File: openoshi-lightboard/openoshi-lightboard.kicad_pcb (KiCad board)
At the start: 2 copper layers, 30 x 30 mm, 26 parts, among them J1 USB_C_Receptacle_PowerOnly_6P, Q1 CSD16301Q2, Q2 CSD16301Q2, Q3 CSD16301Q2, Q4 CSD16301Q2, SW1 SW_Push, SW2 SW_Push, U1 CH32V003FxUx, U2 TLV61070ADBV, U3 MCP73831-3-MC

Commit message: added pictures to readme
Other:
- board text added: "OpenOshi Lightboard v2.0"
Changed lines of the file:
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@@
 			(at 0 3.5 0)
 			(layer "B.SilkS")
+			(hide yes)
 			(effects
 				(font
@@
 		(layer "Edge.Cuts")
 	)
+	(gr_text "OpenOshi Lightboard v2.0"
+		(at 151.65 85.4 0)
+		(layer "B.SilkS")
+		(effects
+			(font
+				(size 0.5 0.5)
+				(thickness 0.1)
+				(bold yes)
+			)
+			(justify left bottom mirror)
+		)
+	)
 	(zone

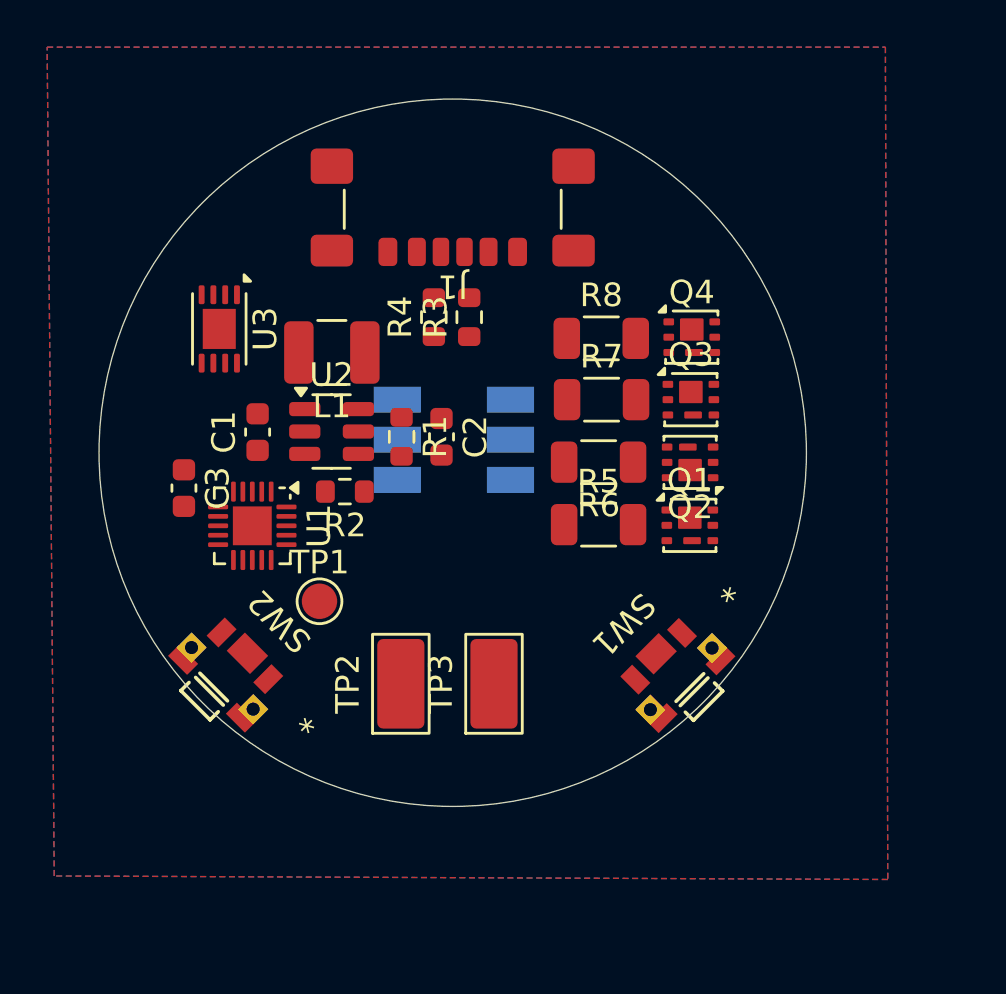
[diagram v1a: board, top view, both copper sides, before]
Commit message: updated readme and part names
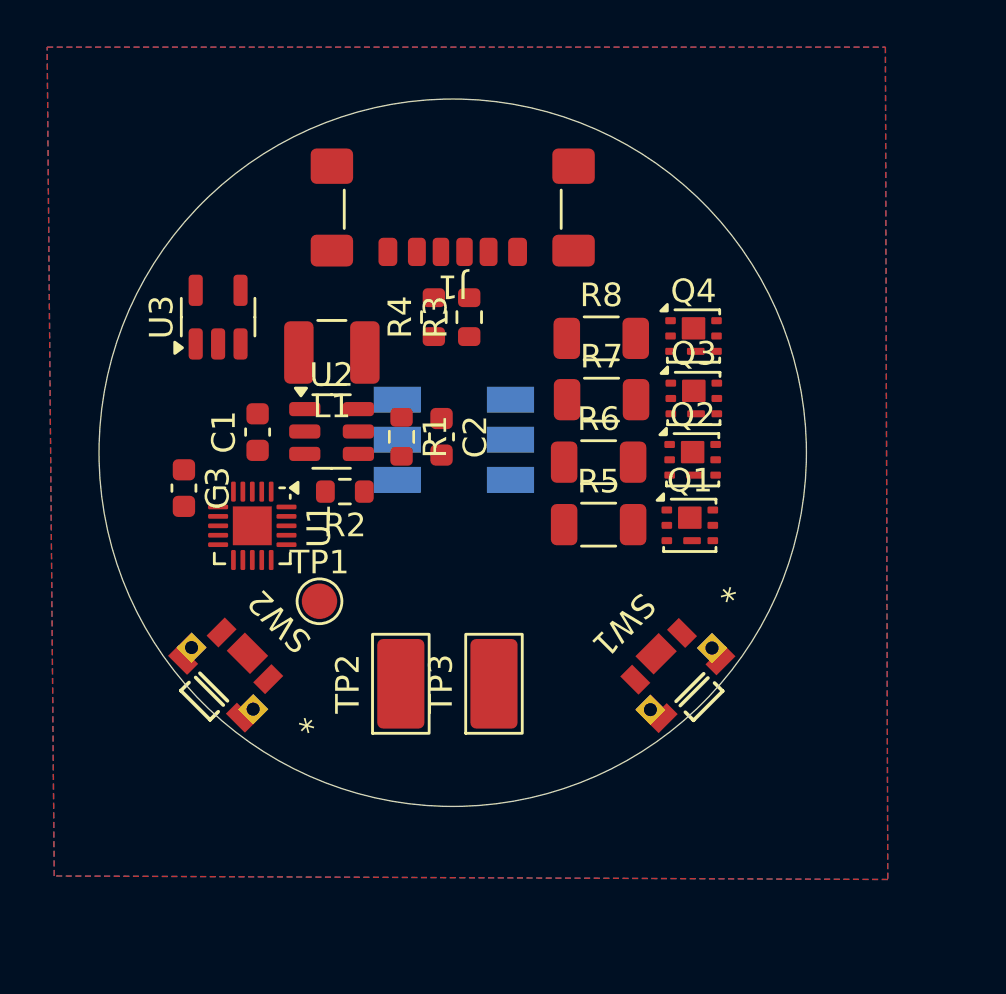
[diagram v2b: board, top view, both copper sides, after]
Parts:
- Q1, Q2, Q3, Q4: value CSD16301Q2 -> CSD17318Q2
- U3: value MCP73831-3-MC -> MCP73831-2-OT; footprint Package_DFN_QFN:DFN-8-1EP_3x2mm_P0.5mm_EP1.7x1.4mm -> Package_TO_SOT_SMD:SOT-23-5
- moved U3 0.50 mm to (136.7, 91.2), turned to 90 degrees
- moved Q2 0.15 mm to (156.8, 97.2), turned to 0 degrees
- moved Q3 0.13 mm to (156.8, 94.6)
- moved Q4 0.09 mm to (156.8, 92.0)
- turned R6 to 0 degrees
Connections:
- U3 pad 1: VBUS -> unconnected-(U3-STAT-Pad1)
- U3 pad 2: VBUS -> GND
- U3 pad 4: +BATT -> VBUS
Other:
- rule pad_to_mask_clearance: 0 -> 0.038

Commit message: added LED
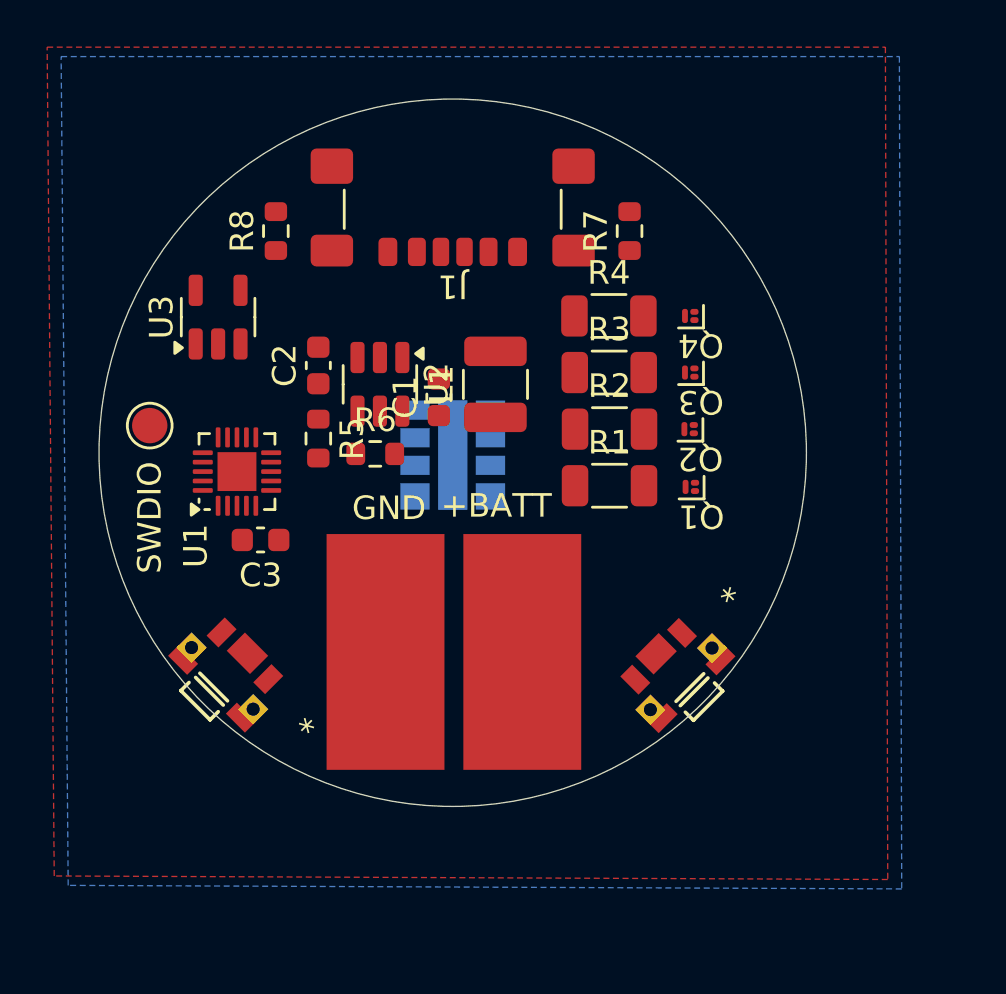
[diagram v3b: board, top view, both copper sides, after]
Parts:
- removed D1: APA102, LED_SMD:LED_RGB_5050-6
- added LED1: L1MC-RGB5080500MP0, openoshi-lightboard:5050RGBW_LUL, B.Cu at (146.6, 97.0)
- L1: value L -> 4.7uH
- Q1, Q2, Q3, Q4: value CSD17318Q2 -> CSD17484F4; footprint Package_SON:Texas_DQK -> Package_DFN_QFN:Texas_PicoStar_DFN-3_0.69x0.60mm
- TP2: value TestPoint -> +BATT; footprint TestPoint:TestPoint_Keystone_5019_Miniature -> Connector_Wire:SolderWirePad_1x01_SMD_5x10mm
- TP3: value TestPoint -> GND; footprint TestPoint:TestPoint_Keystone_5019_Miniature -> Connector_Wire:SolderWirePad_1x01_SMD_5x10mm
- moved TP1 10.4 mm to (133.8, 95.8)
- moved C1 7.83 mm to (146.0, 94.5)
- moved R7 7.72 mm to (154.1, 87.5)
- moved R8 7.63 mm to (139.1, 87.5)
- moved L1 7.07 mm to (148.4, 94.0), turned to 90 degrees
- moved C2 6.04 mm to (140.9, 93.2), turned to 90 degrees
- moved TP2 5.32 mm to (149.6, 105.3), turned to 180 degrees
- moved TP3 4.79 mm to (143.8, 105.3), turned to 180 degrees
- moved C3 3.92 mm to (138.4, 100.6), turned to 0 degrees
- moved R5 3.53 mm to (140.9, 96.3)
- moved U2 2.86 mm to (143.5, 94.0), turned to -90 degrees
- moved U1 2.39 mm to (137.4, 97.7), turned to 90 degrees
- moved R6 2.05 mm to (143.3, 97.0), turned to 0 degrees
- moved R1 1.71 mm to (153.2, 98.3)
- moved Q1 1.63 mm to (156.7, 98.3), turned to 180 degrees
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- renumbered R5 to R1, R6 to R2, R7 to R3, R8 to R4, R1 to R5, R2 to R6, R3 to R7, R4 to R8
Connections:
- net Net-(U2-V_{FB}) renamed /VREG_FB
- Q1 pad 1: Net-(Q1-D-Pad1) -> /G_BLUE
- Q1 pad 2: Net-(Q1-D-Pad1) -> GND
- Q1 pad 3: unconnected-(Q1-G-Pad3) -> Net-(Q1-D)
- Q2 pad 1: Net-(Q2-D-Pad1) -> /G_RED
- Q2 pad 2: Net-(Q2-D-Pad1) -> GND
- Q2 pad 3: unconnected-(Q2-G-Pad3) -> Net-(Q2-D)
- Q3 pad 1: Net-(Q3-D-Pad1) -> /G_GREEN
- Q3 pad 2: Net-(Q3-D-Pad1) -> GND
- Q3 pad 3: unconnected-(Q3-G-Pad3) -> Net-(Q3-D)
- Q4 pad 1: Net-(Q4-D-Pad1) -> /G_WHITE
- Q4 pad 2: Net-(Q4-D-Pad1) -> GND
- Q4 pad 3: unconnected-(Q4-G-Pad3) -> Net-(Q4-D)
- R1 pad 1: unconnected-(R5-Pad1) -> /K_BLUE
- R1 pad 2: Net-(Q1-D-Pad1) -> Net-(Q1-D)
- R2 pad 1: unconnected-(R6-Pad1) -> /K_RED
- R2 pad 2: Net-(Q2-D-Pad1) -> Net-(Q2-D)
- R3 pad 1: unconnected-(R7-Pad1) -> /K_GREEN
- R3 pad 2: Net-(Q3-D-Pad1) -> Net-(Q3-D)
- R4 pad 1: unconnected-(R8-Pad1) -> /K_WHITE
- R4 pad 2: Net-(Q4-D-Pad1) -> Net-(Q4-D)

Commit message: Safety upgrades all around
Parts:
- removed LED1: L1MC-RGB5080500MP0, openoshi-lightboard:5050RGBW_LUL
- added D1: Lumileds_5052RGBW, openoshi-lightboard:LED_Lumileds_5052RGBW_LGA9_5.0x5.2mm_P0.5mm, F.Cu at (150.4, 98.4)
- added R10: 2k, Resistor_SMD:R_0603_1608Metric, F.Cu at (154.4, 97.3)
- added R9: 220, Resistor_SMD:R_0603_1608Metric, F.Cu at (158.3, 97.1)
- J1: footprint Connector_USB:USB_C_Receptacle_GCT_USB4135-GF-A_6P_TopMnt_Horizontal -> Connector_USB:USB_C_Receptacle_GCT_USB4125-xx-x_6P_TopMnt_Horizontal
- L1: value 4.7uH -> L
- Q1, Q2, Q3, Q4: value CSD17484F4 -> PMZ600UNEYL
- R5: renamed from R1; value R -> 118; footprint Resistor_SMD:R_1206_3216Metric -> Resistor_SMD:R_0603_1608Metric
- R6: renamed from R2; value R -> 69.8; footprint Resistor_SMD:R_1206_3216Metric -> Resistor_SMD:R_0603_1608Metric
- R7: renamed from R3; value R -> 69.8; footprint Resistor_SMD:R_1206_3216Metric -> Resistor_SMD:R_0603_1608Metric
- R8: renamed from R4; value R -> 69.8; footprint Resistor_SMD:R_1206_3216Metric -> Resistor_SMD:R_0603_1608Metric
- TP2, TP3: footprint Connector_Wire:SolderWirePad_1x01_SMD_5x10mm -> TestPoint:TestPoint_Keystone_5019_Miniature; moved to B.Cu
- U2: value TLV61070ADBV -> TLV61220
- moved TP1 25.4 mm to (159.2, 95.0), turned to 135 degrees
- moved U1 18.8 mm to (156.1, 100.2), turned to 0 degrees
- moved Q4 18.4 mm to (147.3, 107.0), turned to 90 degrees
- moved U3 18.0 mm to (154.3, 94.8), turned to 180 degrees
- moved C3 17.1 mm to (155.2, 104.0), turned to 90 degrees
- moved Q3 15.5 mm to (148.9, 107.0), turned to 90 degrees
- moved R8 14.8 mm to (147.3, 104.7), turned to -90 degrees
- moved Q2 12.6 mm to (150.6, 107.0), turned to 90 degrees
- moved R7 12.0 mm to (148.9, 104.7), turned to -90 degrees
- moved R4 11.8 mm to (149.2, 93.8)
- moved Q1 9.68 mm to (152.2, 106.9), turned to 90 degrees
- moved TP3 9.38 mm to (151.3, 99.8), turned to 90 degrees
- moved R6 9.19 mm to (150.6, 104.7), turned to -90 degrees
- moved C1 7.81 mm to (139.7, 99.2)
- moved R3 7.09 mm to (150.8, 93.8)
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- renumbered R5 to R1, R6 to R2, R7 to R3, R8 to R4
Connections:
- net /VREG_FB renamed Net-(U2-V_{FB})
- SW1 pad 1: unconnected-(SW1-Pad1) -> /SW1_DET
- SW1 pad 2: unconnected-(SW1-Pad2) -> GND
- SW2 pad 1: unconnected-(SW2-Pad1) -> /SW2_DET
- SW2 pad 2: unconnected-(SW2-Pad2) -> GND
- U1 pad 15: /SWDIO -> Net-(U1-PD1)
- U3 pad 1: unconnected-(U3-STAT-Pad1) -> /CHG_STAT
- U3 pad 5: unconnected-(U3-PROG-Pad5) -> Net-(U3-PROG)
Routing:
- net GND: vias 0 -> 1

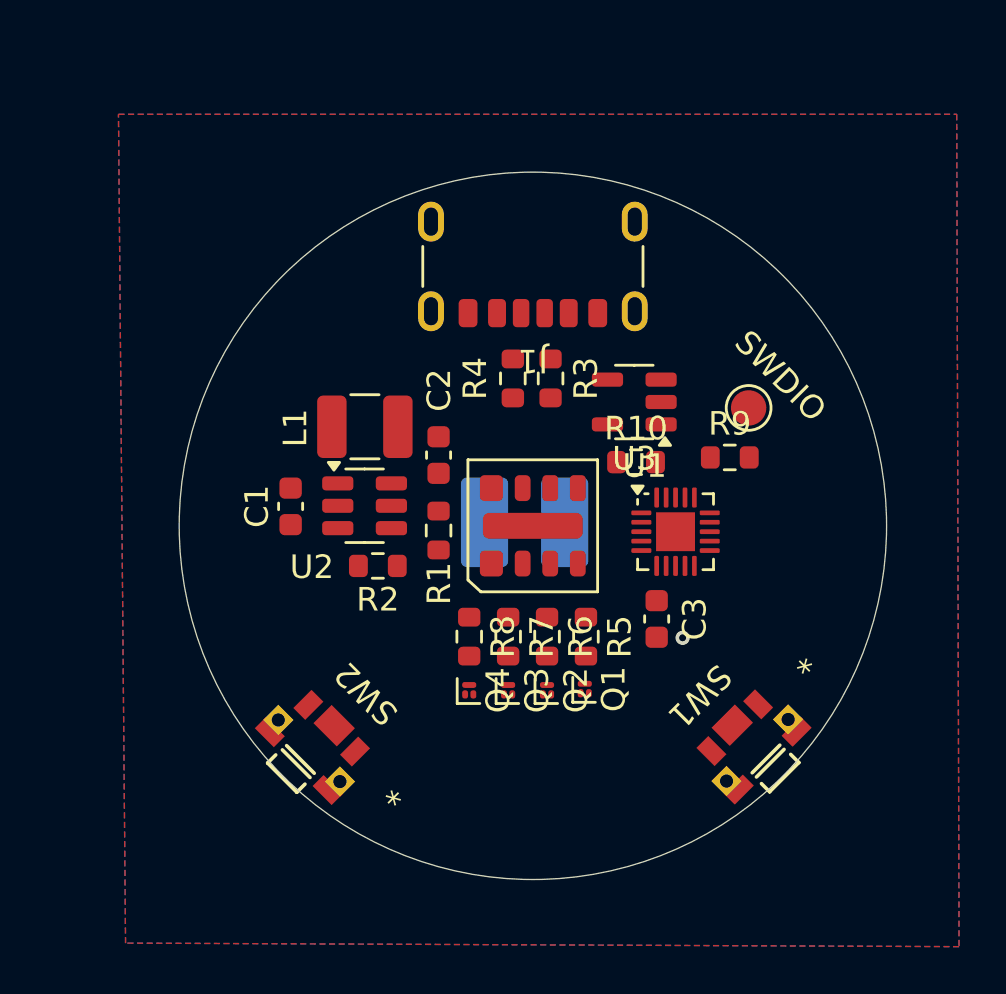
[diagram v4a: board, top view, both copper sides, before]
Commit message: Tentative sch completion, initial layout
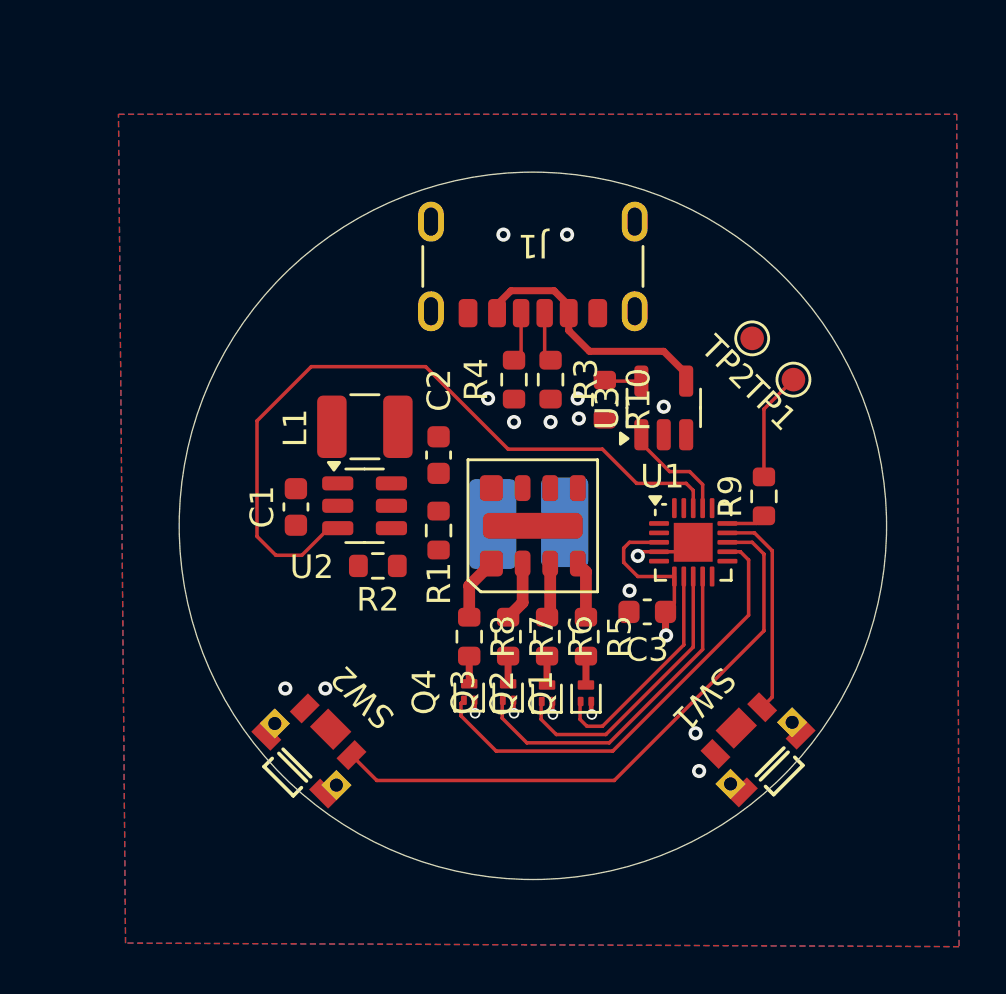
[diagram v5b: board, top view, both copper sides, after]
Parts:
- added TP4: GND, TestPoint:TestPoint_Keystone_5019_Miniature, B.Cu at (148.3, 99.9)
- L1: value L -> 4.7uH
- Q1, Q2, Q3, Q4: value PMZ600UNEYL -> PMZ600UNE; footprint Package_DFN_QFN:Texas_PicoStar_DFN-3_0.69x0.60mm -> Package_TO_SOT_SMD:SOT-883
- R1: value R -> 1Meg
- R10: value 2k -> 2K
- R2: value R -> 127K
- R5: value 118 -> 12.7
- R6: value 69.8 -> 20.0
- R7: value 69.8 -> 11.3
- R8: value 69.8 -> 12.7
- SW1, SW2: value SW_Push -> AKE31A
- TP1: value SWDIO -> SWIO; footprint TestPoint:TestPoint_Pad_D1.5mm -> TestPoint:TestPoint_Pad_D1.0mm
- TP2: value +BATT -> GND; footprint TestPoint:TestPoint_Keystone_5019_Miniature -> TestPoint:TestPoint_Pad_D1.0mm; moved to F.Cu
- TP3: value GND -> +BATT
- U2: value TLV61220 -> TLV61070A
- moved TP2 13.8 mm to (159.3, 92.0), turned to 135 degrees
- moved R10 2.96 mm to (153.1, 94.7), turned to -90 degrees
- moved TP1 2.25 mm to (161.1, 93.8)
- moved R9 2.20 mm to (159.8, 98.8), turned to 90 degrees
- moved U3 1.27 mm to (155.6, 95.0), turned to 90 degrees
- moved U1 0.87 mm to (156.8, 100.7)
- moved C3 0.50 mm to (154.8, 103.7), turned to 0 degrees
- moved C1 0.23 mm to (139.9, 99.2)
- moved SW2 0.21 mm to (140.6, 109.4)
- moved SW1 0.21 mm to (159.4, 109.4)
- moved Q1 0.18 mm to (152.2, 107.1)
- moved Q2 0.12 mm to (150.6, 107.1)
- moved Q3 0.08 mm to (148.9, 107.0)
- moved Q4 0.08 mm to (147.3, 107.0)
- moved R4 0.07 mm to (149.2, 93.8)
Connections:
- net /SWDIO renamed /SWIO
- TP2 pad 1: +BATT -> GND
- TP3 pad 1: GND -> +BATT
- U1 pad 1: unconnected-(U1-PD7-Pad1) -> /MCU_nRST
- U1 pad 12: unconnected-(U1-PC5-Pad12) -> /G_WHITE
- U1 pad 13: unconnected-(U1-PC6-Pad13) -> /SW2_DET
- U1 pad 14: unconnected-(U1-PC7-Pad14) -> /SW1_DET
- U1 pad 17: unconnected-(U1-PD3-Pad17) -> /CHG_STAT
- U1 pad 18: unconnected-(U1-PD4-Pad18) -> /VREG_EN
- U1 pad 3: unconnected-(U1-PA2-Pad3) -> +BATT
- U1 pad 7: unconnected-(U1-PC0-Pad7) -> /G_BLUE
- U1 pad 8: unconnected-(U1-PC1-Pad8) -> /G_RED
- U1 pad 9: unconnected-(U1-PC2-Pad9) -> /G_GREEN
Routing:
- net /VREG_EN: track 0.00 -> 31.5 mm
- net /SW2_DET: track 0.00 -> 25.6 mm
- net /G_WHITE: track 0.00 -> 19.3 mm
- net /G_GREEN: track 0.00 -> 14.4 mm
- net /G_RED: track 0.00 -> 12.0 mm
- net VBUS: track 0.00 -> 11.0 mm
- net /G_BLUE: track 0.00 -> 9.62 mm
- net /SW1_DET: track 0.00 -> 9.03 mm
- net +BATT: track 0.00 -> 7.27 mm, vias 0 -> 1
- net GND: track 0.00 -> 4.84 mm, vias 1 -> 18
- net /CHG_STAT: track 0.00 -> 4.69 mm
- net /SWIO: track 0.00 -> 4.64 mm
- net /K_WHITE: track 0.00 -> 2.66 mm
- net /K_GREEN: track 0.00 -> 2.53 mm
- net /K_BLUE: track 0.00 -> 2.42 mm
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
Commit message: Prepping for large reroute
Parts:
- moved L1 6.83 mm to (139.8, 101.9), turned to -90 degrees
- moved R2 4.50 mm to (143.4, 97.2)
- moved C2 4.05 mm to (145.9, 101.0), turned to -90 degrees
- moved TP4 2.68 mm to (149.1, 102.5), turned to 180 degrees
- moved TP3 2.51 mm to (149.1, 98.8), turned to 0 degrees
- moved R1 2.25 mm to (145.9, 98.0), turned to 90 degrees
- moved C1 1.39 mm to (140.7, 98.0)
- moved U2 1.12 mm to (143.2, 100.2), turned to 90 degrees
- moved Q2 0.20 mm to (150.8, 107.1)
- moved Q3 0.20 mm to (149.2, 107.0)
- moved R6 0.20 mm to (150.8, 104.7)
- moved R7 0.20 mm to (149.2, 104.7)
- moved Q1 0.20 mm to (152.4, 107.1)
- moved Q4 0.20 mm to (147.5, 107.0)
- moved R5 0.20 mm to (152.4, 104.7)
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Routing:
- net +BATT: track 7.27 -> 38.1 mm, vias 1 -> 6
- net +5V: track 0.00 -> 14.7 mm
- net Net-(U2-V_{FB}): track 0.00 -> 3.58 mm
- net Net-(U2-SW): track 0.00 -> 3.55 mm
- net /CHG_STAT: track 4.69 -> 7.85 mm
- net /VREG_EN: track 31.5 -> 30.1 mm
- net GND: track 4.84 -> 6.11 mm, vias 18 -> 22
- added copper zone on B.Cu, net +BATT
- added copper zone on F.Cu, net +BATT

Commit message: Reroute complete
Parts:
- R5, R6, R7, R8: footprint Resistor_SMD:R_0603_1608Metric -> Resistor_SMD:R_1206_3216Metric
- moved U3 13.6 mm to (142.1, 93.5), turned to 0 degrees
- moved R10 11.3 mm to (142.4, 91.0), turned to 180 degrees
- moved C3 4.53 mm to (154.3, 99.2), turned to 90 degrees
- moved R9 2.90 mm to (159.8, 95.8)
- moved TP4 2.83 mm to (147.2, 104.6)
- moved Q4 2.06 mm to (145.9, 108.4)
- moved R8 1.66 mm to (145.9, 105.3)
- moved TP3 1.62 mm to (147.4, 98.6)
- moved U1 1.61 mm to (157.2, 99.2), turned to -90 degrees
- moved Q3 1.54 mm to (148.4, 108.4)
- moved Q1 1.50 mm to (153.2, 108.4)
- moved TP2 1.46 mm to (158.1, 91.3)
- moved TP1 1.39 mm to (159.8, 93.1)
- moved Q2 1.30 mm to (150.8, 108.4)
- moved R5 0.96 mm to (153.2, 105.3)
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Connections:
- U1 pad 10: unconnected-(U1-PC3-Pad10) -> /VREG_EN
- U1 pad 11: unconnected-(U1-PC4-Pad11) -> /G_BLUE
- U1 pad 12: /G_WHITE -> /G_RED
- U1 pad 13: /SW2_DET -> unconnected-(U1-PC6-Pad13)
- U1 pad 14: /SW1_DET -> /G_GREEN
- U1 pad 17: /CHG_STAT -> unconnected-(U1-PD3-Pad17)
- U1 pad 18: /VREG_EN -> /G_WHITE
- U1 pad 19: unconnected-(U1-PD5-Pad19) -> /SW2_DET
- U1 pad 2: unconnected-(U1-PA1-Pad2) -> /CHG_STAT
- U1 pad 20: unconnected-(U1-PD6-Pad20) -> /SW1_DET
- U1 pad 7: /G_BLUE -> unconnected-(U1-PC0-Pad7)
- U1 pad 8: /G_RED -> unconnected-(U1-PC1-Pad8)
- U1 pad 9: /G_GREEN -> unconnected-(U1-PC2-Pad9)
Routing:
- net /CHG_STAT: track 7.85 -> 26.5 mm
- net /VREG_EN: track 30.1 -> 19.9 mm
- net +BATT: track 38.1 -> 30.4 mm
- net /G_WHITE: track 19.2 -> 23.9 mm
- net /G_GREEN: track 14.3 -> 17.9 mm
- net /SW2_DET: track 26.0 -> 29.4 mm
- net Net-(U1-PD1): track 1.68 -> 5.05 mm, vias 0 -> 2
- net /SW1_DET: track 9.24 -> 12.2 mm
- net /SWIO: track 4.64 -> 1.93 mm
- net /G_RED: track 11.9 -> 14.6 mm
- net /G_BLUE: track 9.51 -> 11.4 mm
- net VBUS: track 11.2 -> 12.4 mm
- net GND: track 6.11 -> 7.12 mm, vias 22 -> 24
- net /K_WHITE: track 2.58 -> 3.22 mm
